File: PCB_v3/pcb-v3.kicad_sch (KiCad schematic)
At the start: 8 parts, among them J1 Conn_02x20_Odd_Even, J2 Conn_01x07_Socket, J3 Screw_Terminal_01x03, J4 Screw_Terminal_01x02

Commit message: Updated PCB to V3
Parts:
- removed C1: 100uf, Capacitor_THT:CP_Radial_Tantal_D10.5mm_P5.00mm, symbol Device:C
- removed J3: Screw_Terminal_01x03, Connector_PinHeader_2.54mm:PinHeader_1x03_P2.54mm_Horizontal, symbol Connector:Screw_Terminal_01x03
- removed P1: ~, symbol Cruz_Control_Lib:LC78_05-3.0
- removed U1: ~, symbol Cruz_Control_Lib:PCA_9685
- added Q1: ~, Converter_DCDC:LC78_05-3.0, symbol Cruz_Control_Official_Library:Buck_(12V-5V)
- added U2: ~, Motors:Adafruit PCA9685 rev C (1), symbol Adafruit9685_lib:PCA9685
- C2: footprint (none) -> Connector_AMASS:AMASS_XT60PW-F_1x02_P7.20mm_Horizontal
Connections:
- net +12V: now also C2.1 (Vin), C2.2 (Vout), Q1.1 (Vin)
- net +5V: now also Q1.3 (Vout), U2.28 (VDD)
- net GND: now also Q1.2 (GND), U2.14 (GND), U2.25 (EXTCLK)
- net SCL: now also U2.26 (SCL)
- net SDA: now also U2.27 (SDA)
- no-connect marks 26 -> 33
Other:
- note added: "PCA9685"
- note removed: "SERVO"
- note removed: "Servo Driver"
- moved on the sheet: C2, J4

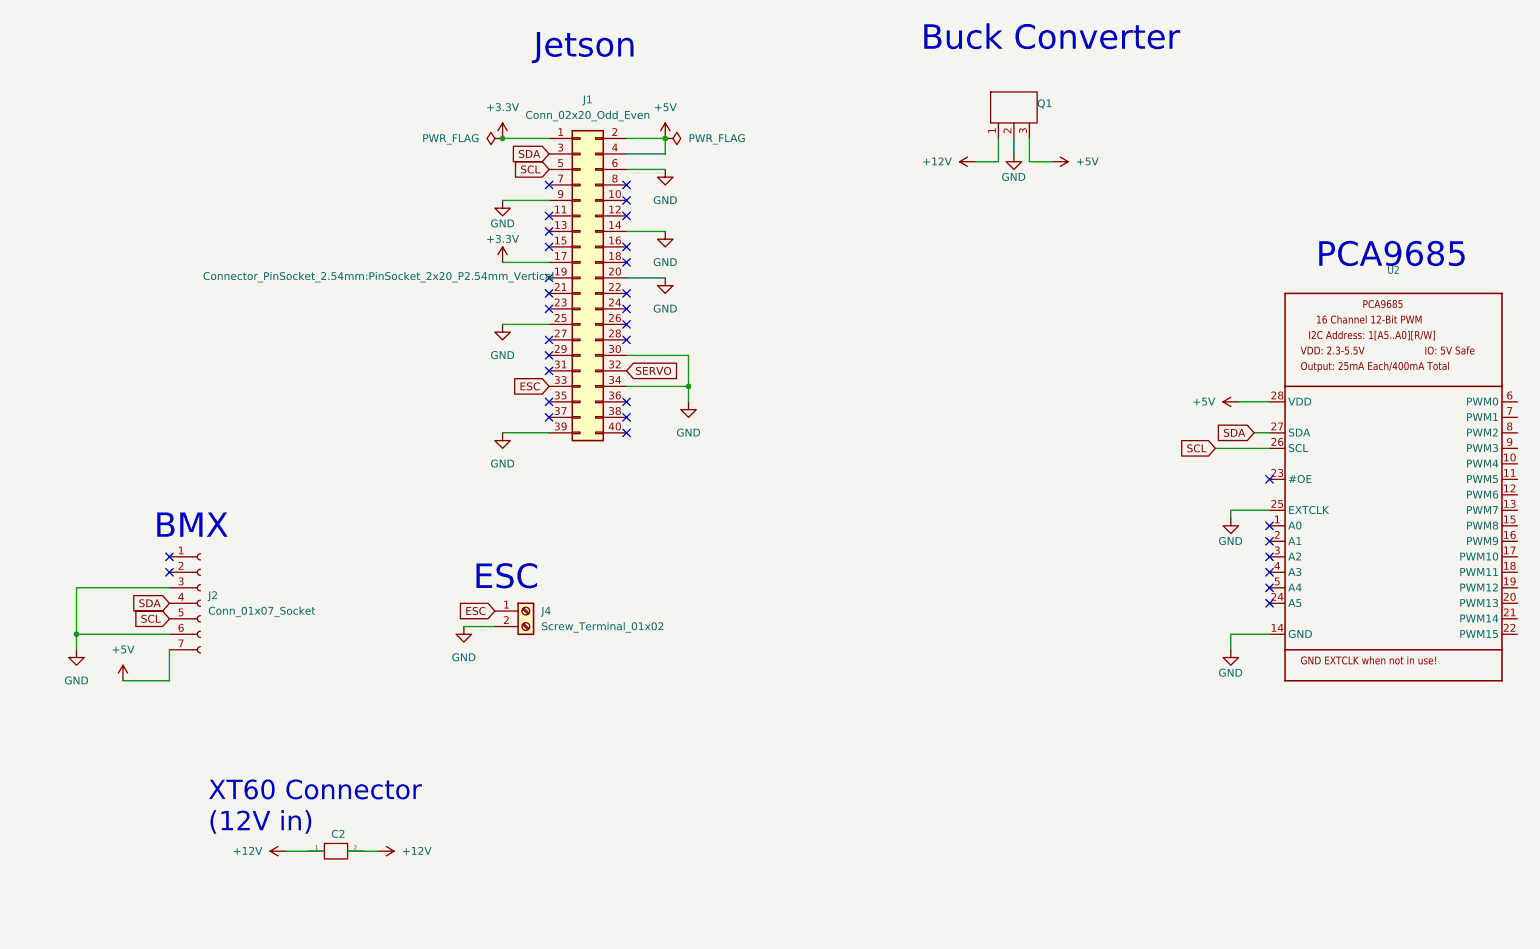
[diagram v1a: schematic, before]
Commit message: completed board with labels included
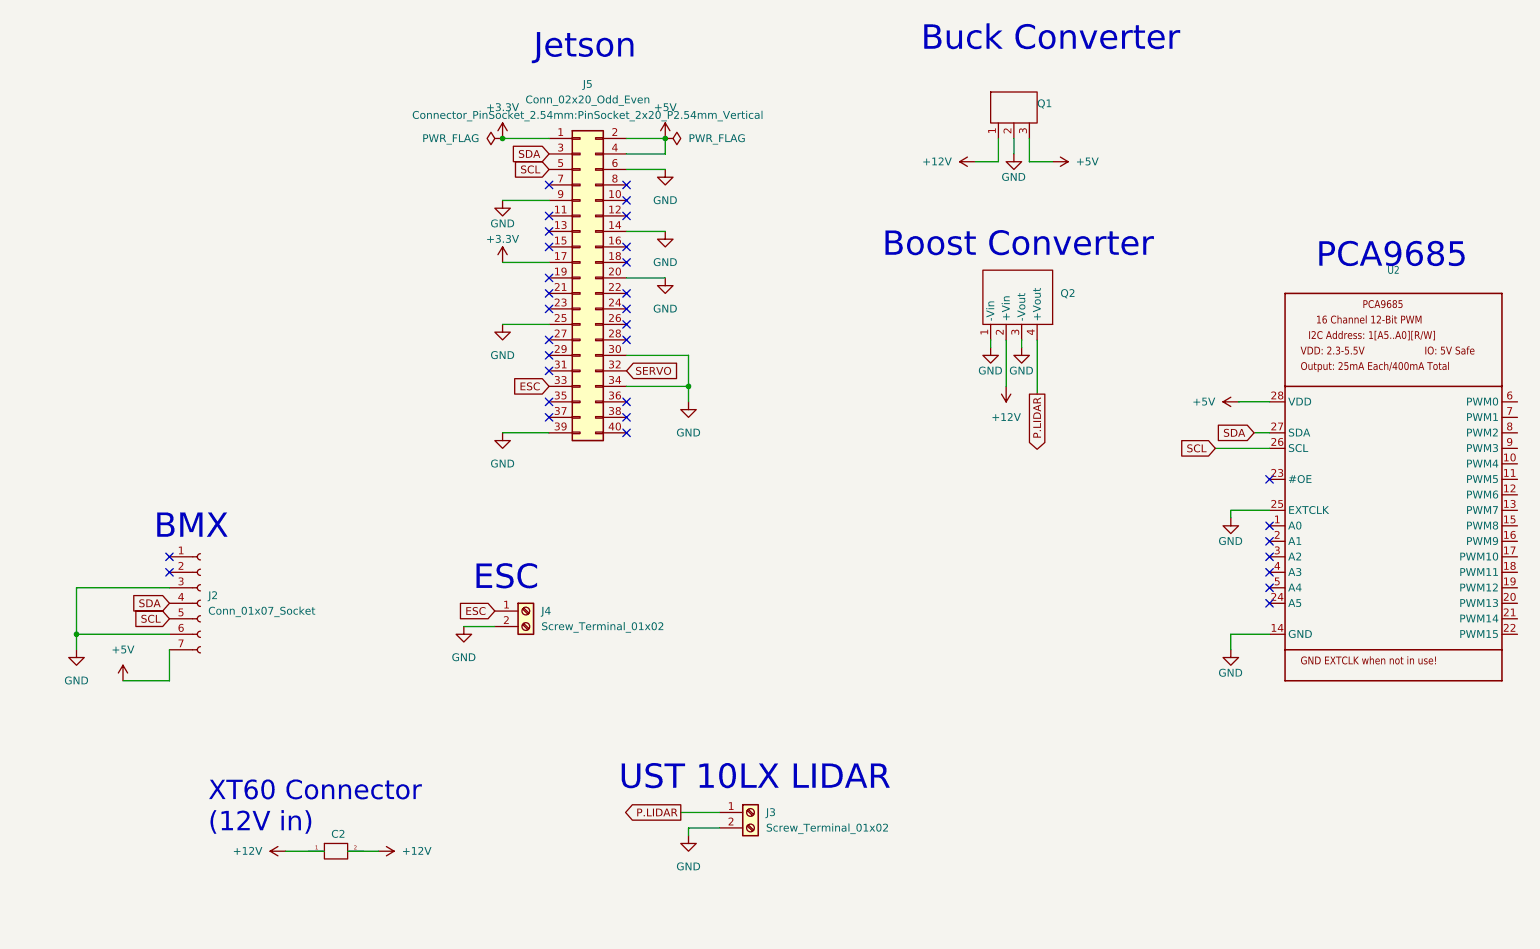
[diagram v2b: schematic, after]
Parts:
- removed J1: Conn_02x20_Odd_Even, Connector_PinSocket_2.54mm:PinSocket_2x20_P2.54mm_Vertical, symbol Connector_Generic:Conn_02x20_Odd_Even
- added J3: Screw_Terminal_01x02, Connector_PinHeader_2.54mm:PinHeader_1x02_P2.54mm_Horizontal, symbol Connector:Screw_Terminal_01x02
- added J5: Conn_02x20_Odd_Even, Connector_PinSocket_2.54mm:PinSocket_2x20_P2.54mm_Vertical, symbol Connector_Generic:Conn_02x20_Odd_Even
- added Q2: ~, Cruz_Control_Footprints:CRE1S Boost Converter, symbol Cruz_Control_Official_Library:Boost_(12V-12V)
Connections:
- net +12V: now also Q2.2 (+Vin)
- net +3.3V: now also J5.1 (Pin_1), J5.17 (Pin_17)
- net +5V: now also J5.2 (Pin_2), J5.4 (Pin_4)
- net ESC: now also J5.33 (Pin_33)
- net GND: now also J3.2 (Pin_2), J5.14 (Pin_14), J5.20 (Pin_20), J5.25 (Pin_25), J5.30 (Pin_30), J5.34 (Pin_34), J5.39 (Pin_39), J5.6 (Pin_6), J5.9 (Pin_9), Q2.1 (-Vin), Q2.3 (-Vout)
- net SCL: now also J5.5 (Pin_5)
- net SDA: now also J5.3 (Pin_3)
- net SERVO: now also J5.32 (Pin_32)
- new net P.LIDAR: J3.1 (Pin_1), Q2.4 (+Vout)
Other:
- note added: "Boost Converter"
- note added: "UST 10LX LIDAR"

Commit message: updated PCB
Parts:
- added J1: Screw_Terminal_01x02, Connector_PinHeader_2.54mm:PinHeader_1x02_P2.54mm_Horizontal, symbol Connector:Screw_Terminal_01x02
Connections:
- net +5V: now also U2.24 (A5)
- net GND: now also J1.2 (Pin_2)
- net SCL: now also U2.4 (A3)
- net SDA: now also U2.3 (A2)
- net P.LIDAR renamed STABLE_12V
- net STABLE_12V: now also J1.1 (Pin_1)
- no-connect marks 33 -> 46

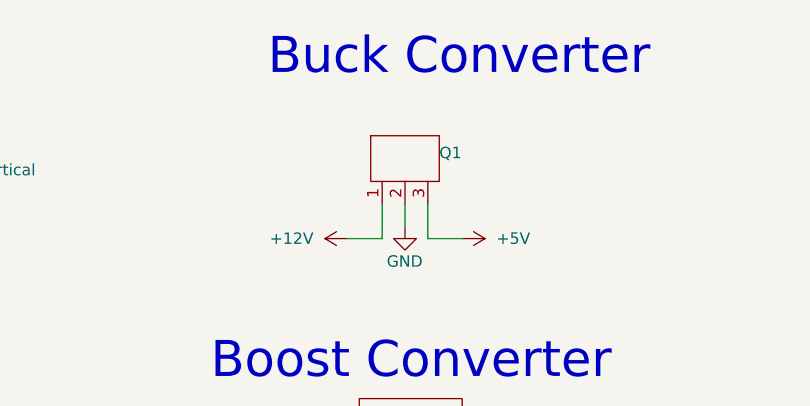
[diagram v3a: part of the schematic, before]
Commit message: added mounting holes to PCB
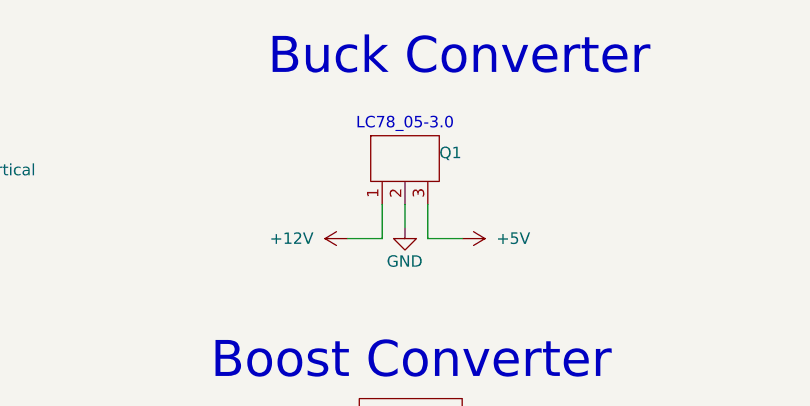
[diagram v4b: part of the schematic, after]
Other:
- note added: "LC78_05-3.0"
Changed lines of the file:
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@@
+		)
+	)
+	(text "LC78_05-3.0"
+		(exclude_from_sim no)
+		(at 185.42 45.72 0)
+		(effects
+			(font
+				(size 1.27 1.27)
+			)
 		)
 	)
